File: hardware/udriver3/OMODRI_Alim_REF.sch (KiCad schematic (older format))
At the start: 16 parts, among them U5 REF6230, U6 OPA388

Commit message: Update of the schematics. Switches on GPIO72 & GPIO84 are missing. J1, J2 & J14 must be merged and connector placement optimized. TCXO must be changed from 20MHz to 25MHz for EtherCAT compatibility. PCB is partially routed in 6-Layers (mainly power supplies and and transistors). 8-Layers will be necessary.
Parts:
- removed C24, C32, C33: 100nF, Capacitor_SMD:C_0201_0603Metric, symbol Device:C
- removed C25, C30, C31: 10uF, Capacitor_SMD:C_0603_1608Metric, symbol Device:C
- removed R10, R11, R12: 0.1, Resistor_SMD:R_0201_0603Metric, symbol Device:R
- removed U5: REF6230, Package_SO:VSSOP-8_3.0x3.0mm_P0.65mm, symbol omodri_lib:REF6230
- removed U6: OPA388, Package_TO_SOT_SMD:TSOT-23-5, symbol omodri_lib:OPA388
- added U5: LT6654AIS6-3, Package_TO_SOT_SMD:TSOT-23-6, symbol omodri_lib:LT6654AIS6-3
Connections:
- wire segments 55 -> 21
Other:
- moved on the sheet: C26, C27, C28, C29, TP9

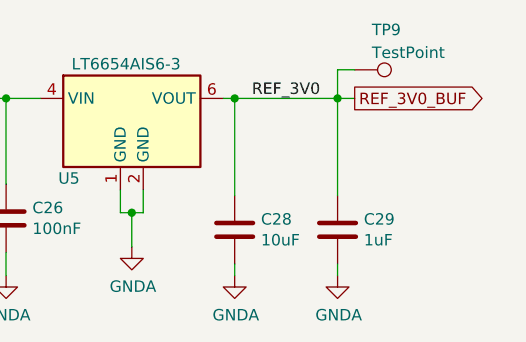
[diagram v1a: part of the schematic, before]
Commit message: First release of the fully routed OMODRI PCB from LAAS. (8 layers)
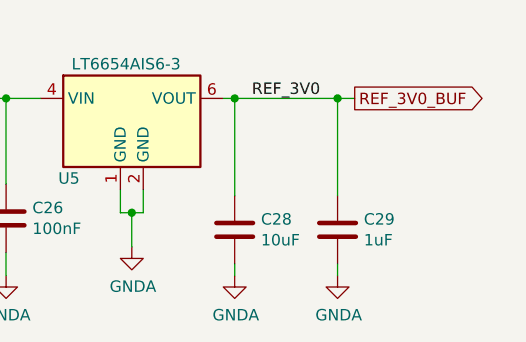
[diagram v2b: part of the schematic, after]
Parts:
- removed TP9: TestPoint, TestPoint:TestPoint_Pad_D1.0mm, symbol Connector:TestPoint
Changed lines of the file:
@@
 $Descr A4 11693 8268
 encoding utf-8
-Sheet 6 17
+Sheet 6 19
 Title "Open MOtor DRiver Initiative (OMODRI)"
 Date ""
@@
 	1    0    0    -1
 $EndComp
-$Comp
-L Connector:TestPoint TP?
-U 1 1 5F7B8A07
-P 7125 3050
-AR Path="/5F310311/5F7B8A07" Ref="TP?"  Part="1"
-AR Path="/5F3255E8/5F7B8A07" Ref="TP?"  Part="1"
-AR Path="/5F387075/5F7B8A07" Ref="TP?"  Part="1"
-AR Path="/5F7B8A07" Ref="TP?"  Part="1"
-AR Path="/5F3A3F16/5F7B8A07" Ref="TP?"  Part="1"
-AR Path="/5F3A3F16/5F5C0183/5F7B8A07" Ref="TP9"  Part="1"
-F 0 "TP9" V 6950 3125 50  0000 L CNN
-F 1 "TestPoint" V 7050 3125 50  0000 L CNN
-F 2 "TestPoint:TestPoint_Pad_D1.0mm" H 7325 3050 50  0001 C CNN
-F 3 "~" H 7325 3050 50  0001 C CNN
-	1    7125 3050
-	0    1    1    0
-$EndComp
 Wire Wire Line
 	6550 3175 6600 3175
@@
 	7050 3175 7125 3175
 Wire Wire Line
-	7125 3050 7050 3050
-Wire Wire Line
-	7050 3050 7050 3175
-Wire Wire Line
 	5025 3175 5200 3175

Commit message: Release 1.1 - Update components values + BOM - Update of J1 pins affectation now matching J2 distribution. - Update gerber files with missing inner layers - Few updates of the PCB layout (J2 redraw + decoupling cap)
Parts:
- C26: DigiKey 490-14450-1-ND -> 490-14571-1-ND; Farnell 2990681 -> 3790414; Mouser 81-GRM033C71A104KE4D -> 81-GRM033R61E104KE4J; Part No GRM033C71A104KE14D -> GRM033R61E104KE14J; RS 185-1751 -> 185-2066
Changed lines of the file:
@@
 F 1 "100nF" H 5715 3655 50  0000 L CNN
 F 2 "Capacitor_SMD:C_0201_0603Metric" H 5638 3550 50  0001 C CNN
-F 3 "https://www.murata.com/en-eu/products/productdetail?partno=GRM033C71A104KE14%23" H 5600 3700 50  0001 C CNN
-F 4 "490-14450-1-ND" H 5600 3700 50  0001 C CNN "DigiKey"
-F 5 "2990681" H 5600 3700 50  0001 C CNN "Farnell"
-F 6 "81-GRM033C71A104KE4D" H 5600 3700 50  0001 C CNN "Mouser"
-F 7 "GRM033C71A104KE14D" H 5600 3700 50  0001 C CNN "Part No"
-F 8 "185-1751" H 5600 3700 50  0001 C CNN "RS"
+F 3 "https://www.murata.com/en-eu/products/productdetail?partno=GRM033C71A104KE14%23." H 5600 3700 50  0001 C CNN
+F 4 "490-14571-1-ND" H 5600 3700 50  0001 C CNN "DigiKey"
+F 5 "3790414" H 5600 3700 50  0001 C CNN "Farnell"
+F 6 "81-GRM033R61E104KE4J" H 5600 3700 50  0001 C CNN "Mouser"
+F 7 "GRM033R61E104KE14J" H 5600 3700 50  0001 C CNN "Part No"
+F 8 "185-2066" H 5600 3700 50  0001 C CNN "RS"
 F 9 "10V" H 5600 3700 50  0001 C CNN "Rated Voltage"
 	1    5600 3700
